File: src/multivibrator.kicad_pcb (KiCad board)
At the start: 2 copper layers, 47 x 31.8 mm, 11 parts, among them CON1 BARREL_JACK, Q1 Q_NPN_EBC, Q2 Q_NPN_EBC

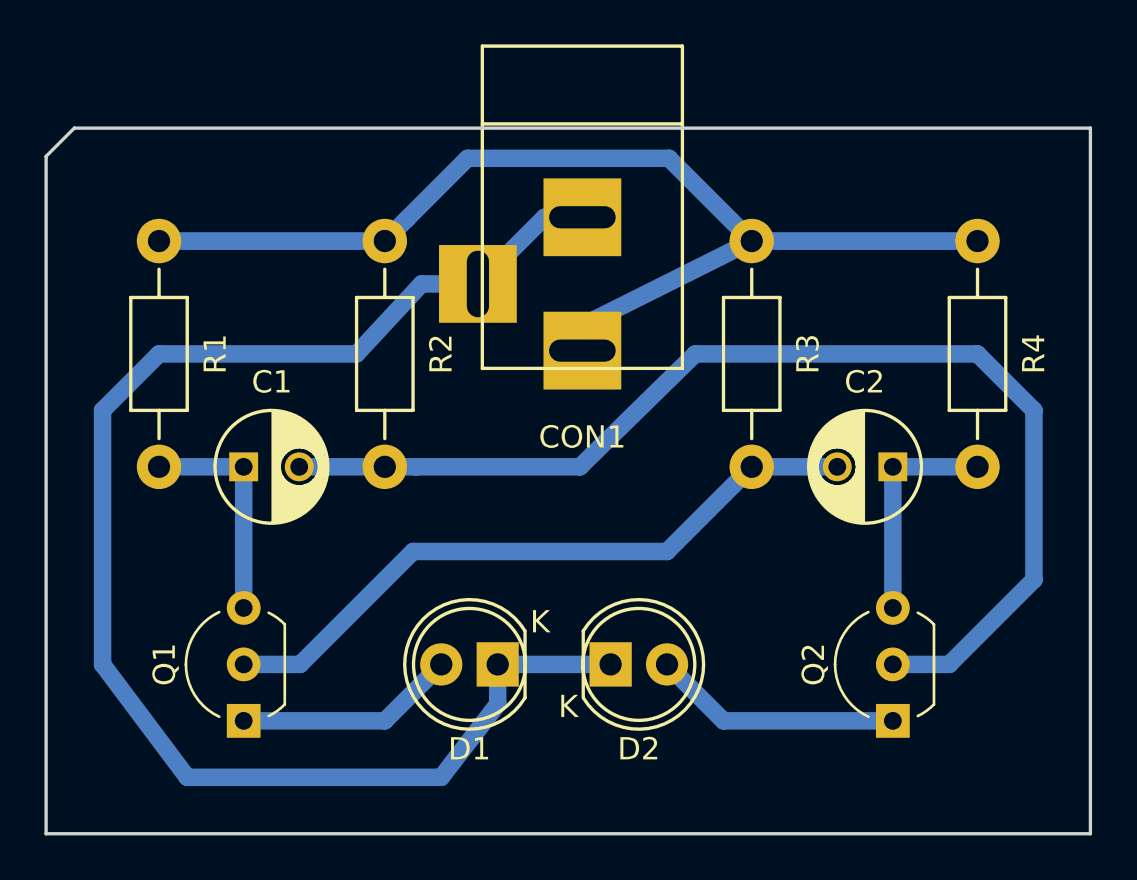
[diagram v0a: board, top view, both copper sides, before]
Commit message: use smaller connector
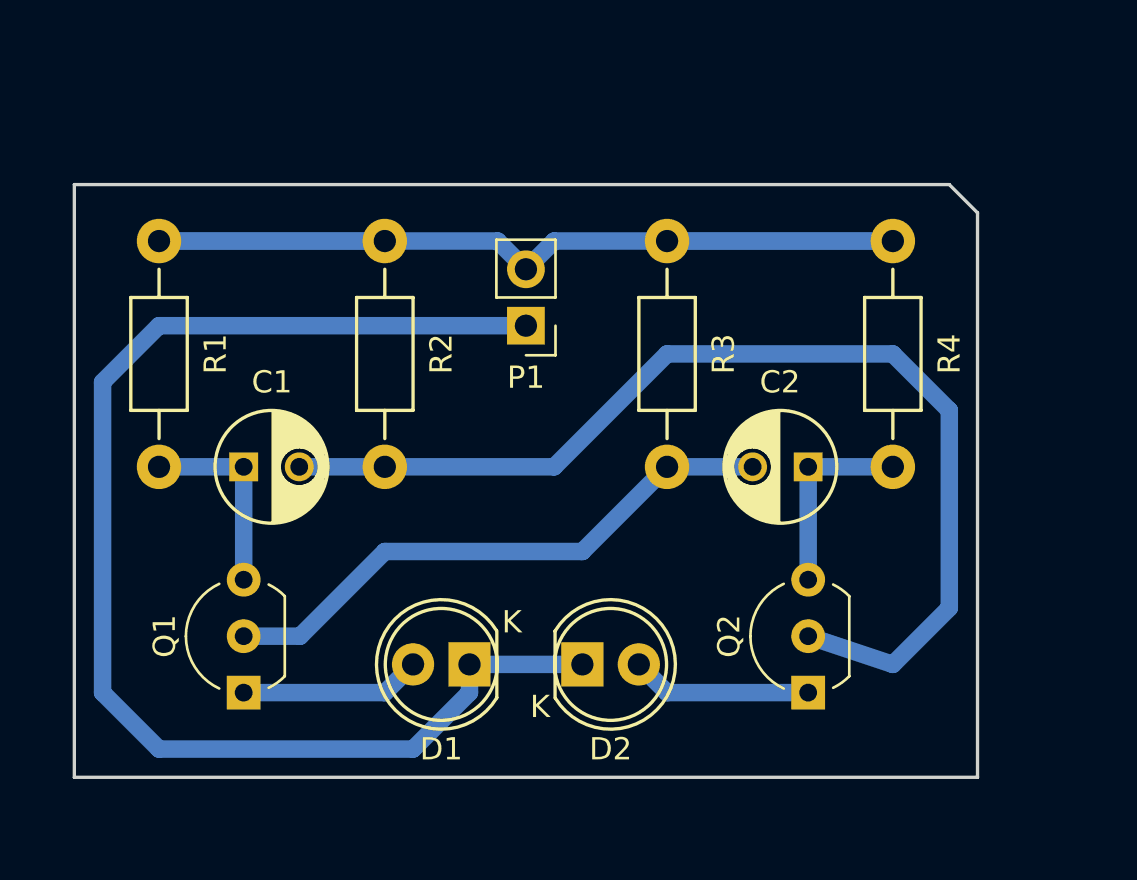
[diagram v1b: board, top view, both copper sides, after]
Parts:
- removed CON1: BARREL_JACK, Connect:BARREL_JACK
- added P1: CONN_01X02, Socket_Strips:Socket_Strip_Straight_1x02_Pitch2.54mm, F.Cu at (99.1, 68.6)
- moved Q2 4.02 mm to (111.8, 85.1)
- moved R3 3.81 mm to (105.4, 64.8)
- moved R4 3.81 mm to (115.6, 64.8)
- moved C2 3.81 mm to (111.8, 74.9)
- moved D1 1.27 mm to (96.5, 83.8)
- moved D2 1.27 mm to (101.6, 83.8)
- moved Q1 1.27 mm to (86.4, 85.1)
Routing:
- net VCC: track 49.6 -> 34.1 mm
- net GND: track 65.5 -> 59.0 mm
- net Net-(C2-Pad2): track 30.4 -> 26.1 mm
- net Net-(D2-Pad2): track 11.2 -> 8.15 mm
- net Net-(C1-Pad2): track 51.7 -> 48.9 mm
- net Net-(D1-Pad2): track 9.94 -> 8.15 mm
- net Net-(C2-Pad1): track 10.2 -> 8.89 mm
- net Net-(C1-Pad1): track 10.2 -> 8.89 mm
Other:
- board size 47 x 31.8 mm -> 40.6 x 26.7 mm

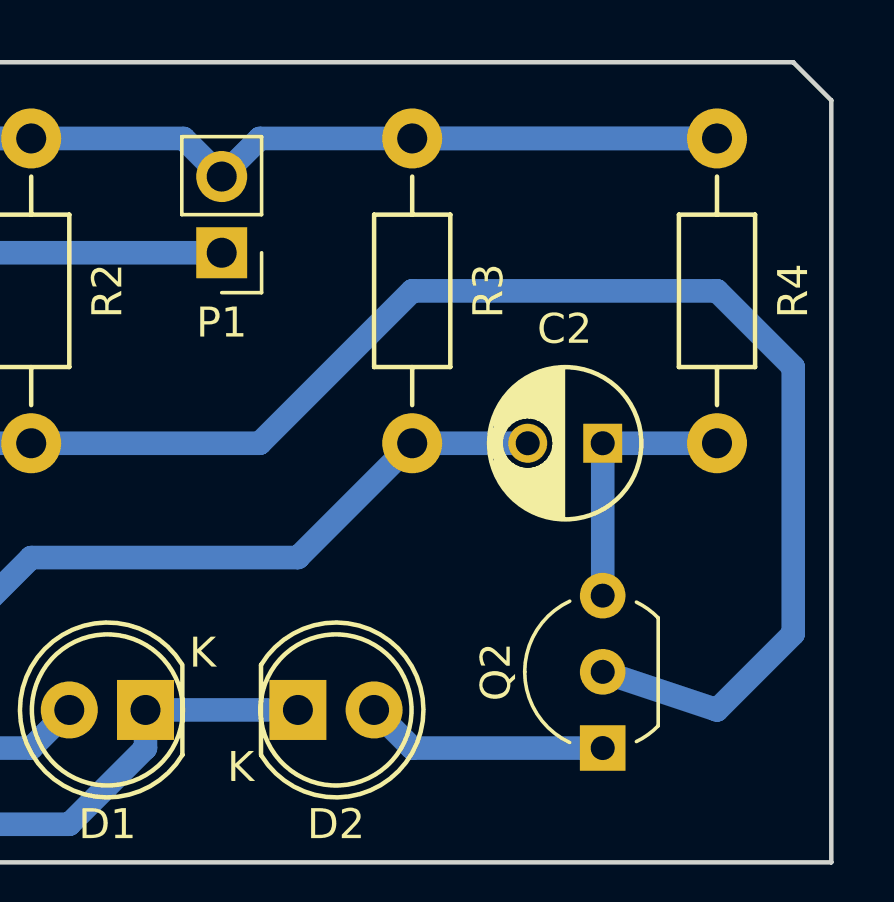
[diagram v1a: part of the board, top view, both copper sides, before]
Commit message: update kicad, rotate connector, clean up trace
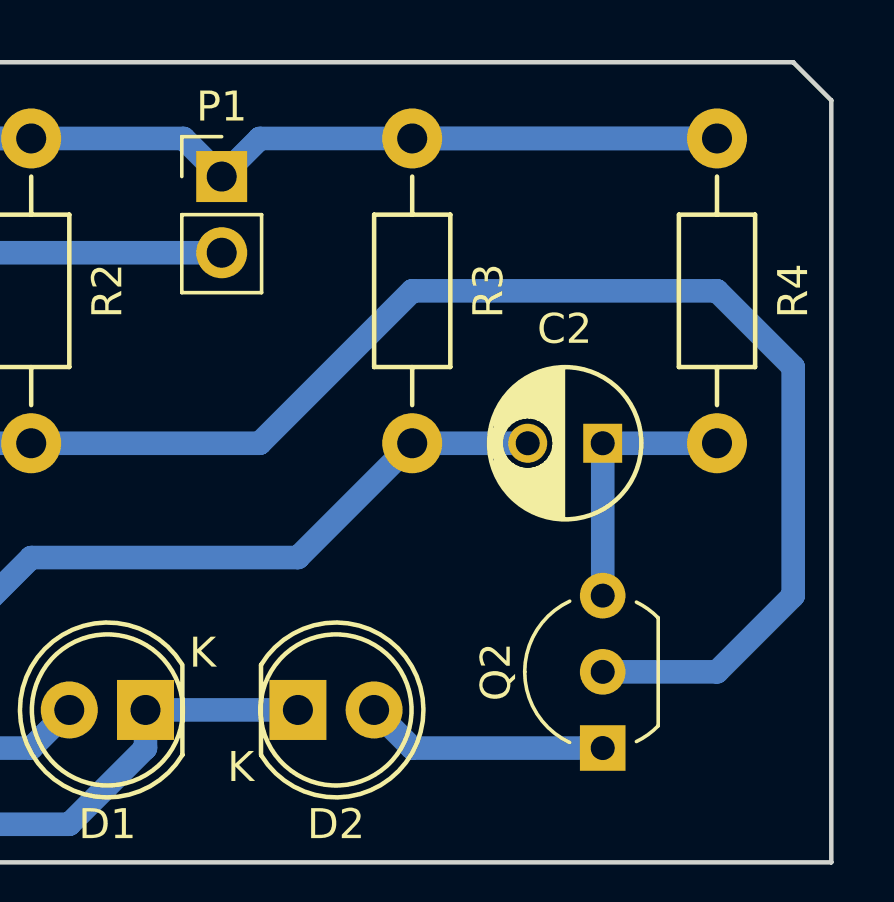
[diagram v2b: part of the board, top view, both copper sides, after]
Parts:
- moved P1 2.54 mm to (99.1, 66.0), turned to 0 degrees
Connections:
- P1 pad 1: GND -> VCC
- P1 pad 2: VCC -> GND
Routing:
- net Net-(C1-Pad2): track 48.9 -> 47.4 mm
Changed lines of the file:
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@@
-(kicad_pcb (version 4) (host pcbnew 4.0.4+e1-6308~48~ubuntu14.04.1-stable)
+(kicad_pcb (version 4) (host pcbnew 4.0.6-e0-6349~53~ubuntu14.04.1)
   (general
     (links 16)
     (no_connects 0)
-    (area 77.394999 59.614999 124.535001 91.515001)
+    (area 78.664999 62.154999 119.455001 88.975001)
     (thickness 1.6)
     (drawings 5)
@@
   )
   (module Socket_Strips:Socket_Strip_Straight_1x02_Pitch2.54mm (layer F.Cu)
-    (at 99.06 68.58 180)
+    (at 99.06 66.04)
     (descr "Through hole straight socket strip, 1x02, 2.54mm pitch, single row")
     (tags "Through hole socket strip THT 1x02 2.54mm single row")
-    (fp_text reference P1 (at 0 -2.33 180) (layer F.SilkS)
-      (effects (font (size 1 1) (thickness 0.15)))
-    )
-    (fp_text value CONN_01X02 (at 0 4.87 180) (layer F.Fab)
+    (fp_text reference P1 (at 0 -2.33) (layer F.SilkS)
+      (effects (font (size 1 1) (thickness 0.15)))
+    )
+    (fp_text value CONN_01X02 (at 0 4.87) (layer F.Fab)
       (effects (font (size 1 1) (thickness 0.15)))
     )
@@
     (fp_line (start 1.8 4.35) (end 1.8 -1.8) (layer F.CrtYd) (width 0.05))
     (fp_line (start 1.8 -1.8) (end -1.8 -1.8) (layer F.CrtYd) (width 0.05))
-    (fp_text user %R (at 0 -2.33 180) (layer F.Fab)
-      (effects (font (size 1 1) (thickness 0.15)))
-    )
-    (pad 1 thru_hole rect (at 0 0 180) (size 1.7 1.7) (drill 1) (layers *.Cu *.Mask)
+    (fp_text user %R (at 0 -2.33) (layer F.Fab)
+      (effects (font (size 1 1) (thickness 0.15)))
+    )
+    (pad 1 thru_hole rect (at 0 0) (size 1.7 1.7) (drill 1) (layers *.Cu *.Mask)
+      (net 8 VCC))
+    (pad 2 thru_hole oval (at 0 2.54) (size 1.7 1.7) (drill 1) (layers *.Cu *.Mask)
       (net 5 GND))
-    (pad 2 thru_hole oval (at 0 2.54 180) (size 1.7 1.7) (drill 1) (layers *.Cu *.Mask)
-      (net 8 VCC))
     (model ${KISYS3DMOD}/Socket_Strips.3dshapes/Socket_Strip_Straight_1x02_Pitch2.54mm.wrl
       (at (xyz 0 -0.05 0))
@@
   (gr_line (start 119.38 63.5) (end 118.11 62.23) (angle 90) (layer Edge.Cuts) (width 0.15))
   (gr_line (start 119.38 88.9) (end 119.38 63.5) (angle 90) (layer Edge.Cuts) (width 0.15))
-  (segment (start 92.71 74.93) (end 100.33 74.93) (width 0.7874) (layer B.Cu) (net 1))
-  (segment (start 115.57 83.82) (end 111.76 82.55) (width 0.7874) (layer B.Cu) (net 1) (status 20))
-  (segment (start 118.11 81.28) (end 115.57 83.82) (width 0.7874) (layer B.Cu) (net 1))
-  (segment (start 118.11 72.39) (end 118.11 81.28) (width 0.7874) (layer B.Cu) (net 1))
+  (segment (start 92.71 74.93) (end 100.33 74.93) (width 0.7874) (layer B.Cu) (net 1) (status 400000))
+  (segment (start 115.57 82.55) (end 111.76 82.55) (width 0.7874) (layer B.Cu) (net 1) (status 800000))
+  (segment (start 118.11 80.01) (end 115.57 82.55) (width 0.7874) (layer B.Cu) (net 1))
+  (segment (start 118.11 72.39) (end 118.11 80.01) (width 0.7874) (layer B.Cu) (net 1))
   (segment (start 115.57 69.85) (end 118.11 72.39) (width 0.7874) (layer B.Cu) (net 1))
   (segment (start 105.41 69.85) (end 115.57 69.85) (width 0.7874) (layer B.Cu) (net 1))
@@
   (segment (start 82.55 74.93) (end 86.36 74.93) (width 0.7874) (layer B.Cu) (net 2))
   (segment (start 86.36 74.93) (end 86.36 80.01) (width 0.7874) (layer B.Cu) (net 2) (status 20))
-  (segment (start 105.41 74.93) (end 101.6 78.74) (width 0.7874) (layer B.Cu) (net 3) (status 400000))
-  (segment (start 88.9 82.55) (end 86.36 82.55) (width 0.7874) (layer B.Cu) (net 3) (status 800000))
+  (segment (start 105.41 74.93) (end 101.6 78.74) (width 0.7874) (layer B.Cu) (net 3))
+  (segment (start 88.9 82.55) (end 86.36 82.55) (width 0.7874) (layer B.Cu) (net 3))
   (segment (start 92.71 78.74) (end 88.9 82.55) (width 0.7874) (layer B.Cu) (net 3))
   (segment (start 101.6 78.74) (end 92.71 78.74) (width 0.7874) (layer B.Cu) (net 3))
@@
   (segment (start 115.57 74.93) (end 111.76 74.93) (width 0.7874) (layer B.Cu) (net 4) (status 10))
   (segment (start 111.76 74.93) (end 111.76 80.01) (width 0.7874) (layer B.Cu) (net 4) (status 20))
-  (segment (start 99.06 68.58) (end 82.55 68.58) (width 0.7874) (layer B.Cu) (net 5) (status 400000))
-  (segment (start 96.52 85.09) (end 96.52 83.82) (width 0.7874) (layer B.Cu) (net 5) (status 800000))
+  (segment (start 96.52 85.09) (end 96.52 83.82) (width 0.7874) (layer B.Cu) (net 5))
   (segment (start 93.98 87.63) (end 96.52 85.09) (width 0.7874) (layer B.Cu) (net 5))
   (segment (start 82.55 87.63) (end 93.98 87.63) (width 0.7874) (layer B.Cu) (net 5))
   (segment (start 80.01 85.09) (end 82.55 87.63) (width 0.7874) (layer B.Cu) (net 5))
   (segment (start 80.01 71.12) (end 80.01 85.09) (width 0.7874) (layer B.Cu) (net 5))
+  (segment (start 96.52 83.82) (end 101.6 83.82) (width 0.7874) (layer B.Cu) (net 5) (status 20))
   (segment (start 82.55 68.58) (end 80.01 71.12) (width 0.7874) (layer B.Cu) (net 5))
-  (segment (start 96.52 83.82) (end 101.6 83.82) (width 0.7874) (layer B.Cu) (net 5) (status 20))
-  (segment (start 86.36 85.09) (end 92.71 85.09) (width 0.7874) (layer B.Cu) (net 6) (status 400000))
-  (segment (start 92.71 85.09) (end 93.98 83.82) (width 0.7874) (layer B.Cu) (net 6) (status 800000))
-  (segment (start 111.76 85.09) (end 105.41 85.09) (width 0.7874) (layer B.Cu) (net 7) (status 400000))
-  (segment (start 105.41 85.09) (end 104.14 83.82) (width 0.7874) (layer B.Cu) (net 7) (status 800000))
+  (segment (start 99.06 68.58) (end 82.55 68.58) (width 0.7874) (layer B.Cu) (net 5))
+  (segment (start 86.36 85.09) (end 92.71 85.09) (width 0.7874) (layer B.Cu) (net 6))
+  (segment (start 92.71 85.09) (end 93.98 83.82) (width 0.7874) (layer B.Cu) (net 6))
+  (segment (start 111.76 85.09) (end 105.41 85.09) (width 0.7874) (layer B.Cu) (net 7))
+  (segment (start 105.41 85.09) (end 104.14 83.82) (width 0.7874) (layer B.Cu) (net 7))
+  (segment (start 100.33 64.77) (end 99.06 66.04) (width 0.7874) (layer B.Cu) (net 8))
+  (segment (start 97.79 64.77) (end 99.06 66.04) (width 0.7874) (layer B.Cu) (net 8))
   (segment (start 105.41 64.77) (end 100.33 64.77) (width 0.7874) (layer B.Cu) (net 8))
-  (segment (start 100.33 64.77) (end 99.06 66.04) (width 0.7874) (layer B.Cu) (net 8))
   (segment (start 92.71 64.77) (end 97.79 64.77) (width 0.7874) (layer B.Cu) (net 8))
-  (segment (start 97.79 64.77) (end 99.06 66.04) (width 0.7874) (layer B.Cu) (net 8))
   (segment (start 92.71 64.77) (end 82.55 64.77) (width 0.8001) (layer B.Cu) (net 8) (status 20))
   (segment (start 115.57 64.77) (end 105.41 64.77) (width 0.8001) (layer B.Cu) (net 8) (status 10))
